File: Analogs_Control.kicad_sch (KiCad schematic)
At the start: 23 parts, among them U801 LM358

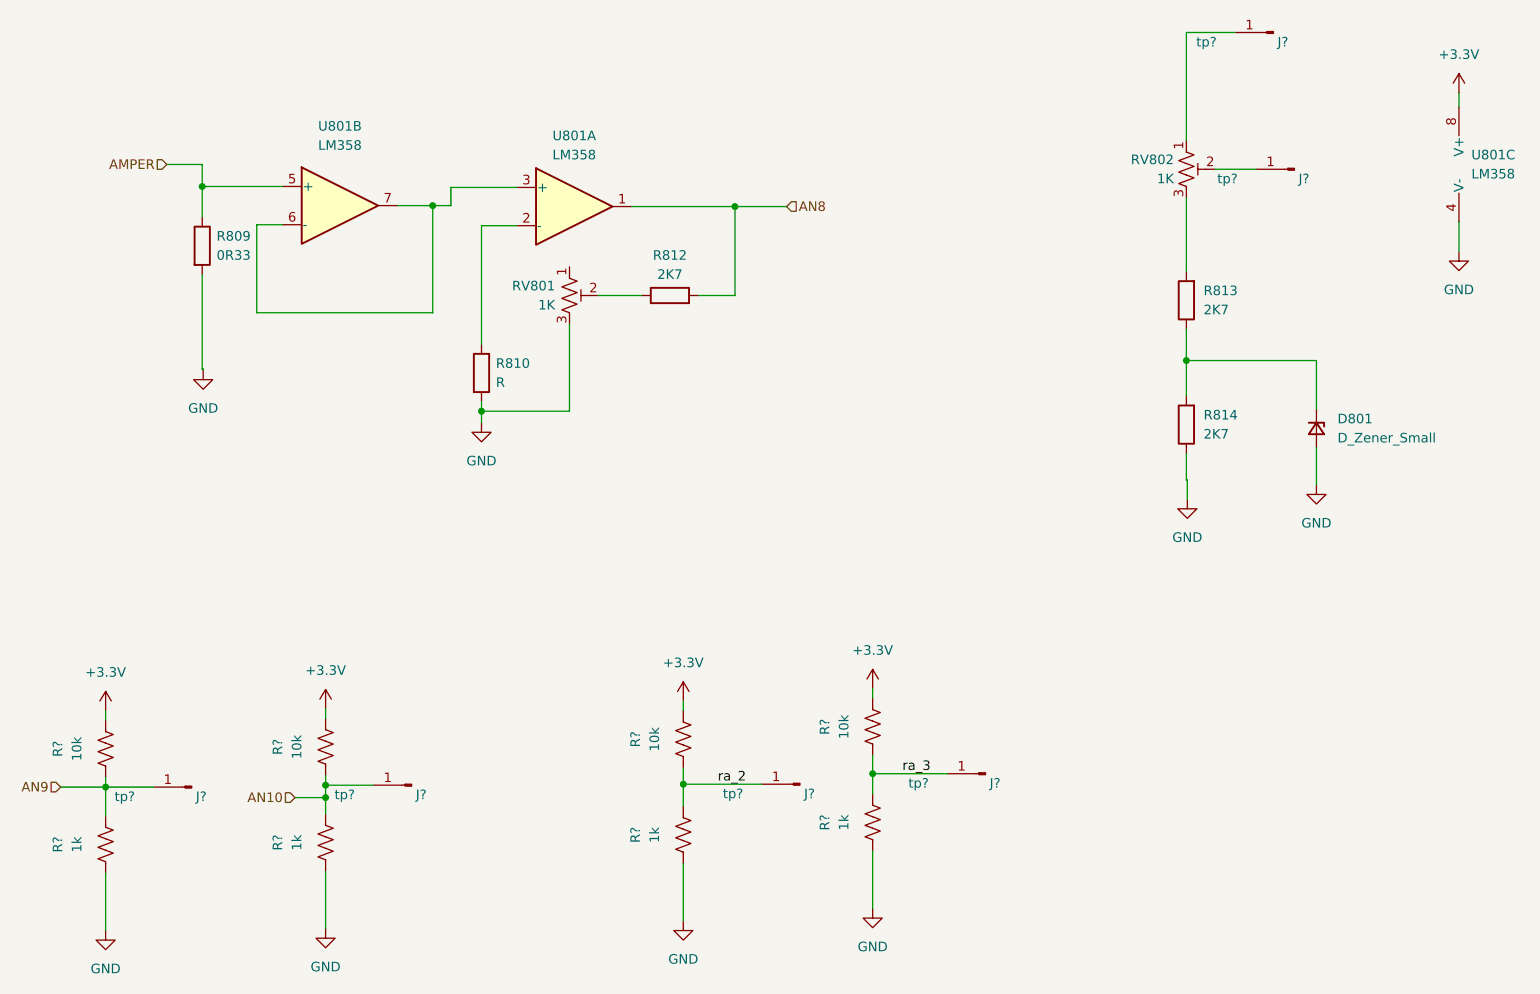
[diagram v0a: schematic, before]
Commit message: feat: agregar hierarchical_labels con nombres correctos a oS_AnaloDev (DiscoveryAnalog3) - 30 pines
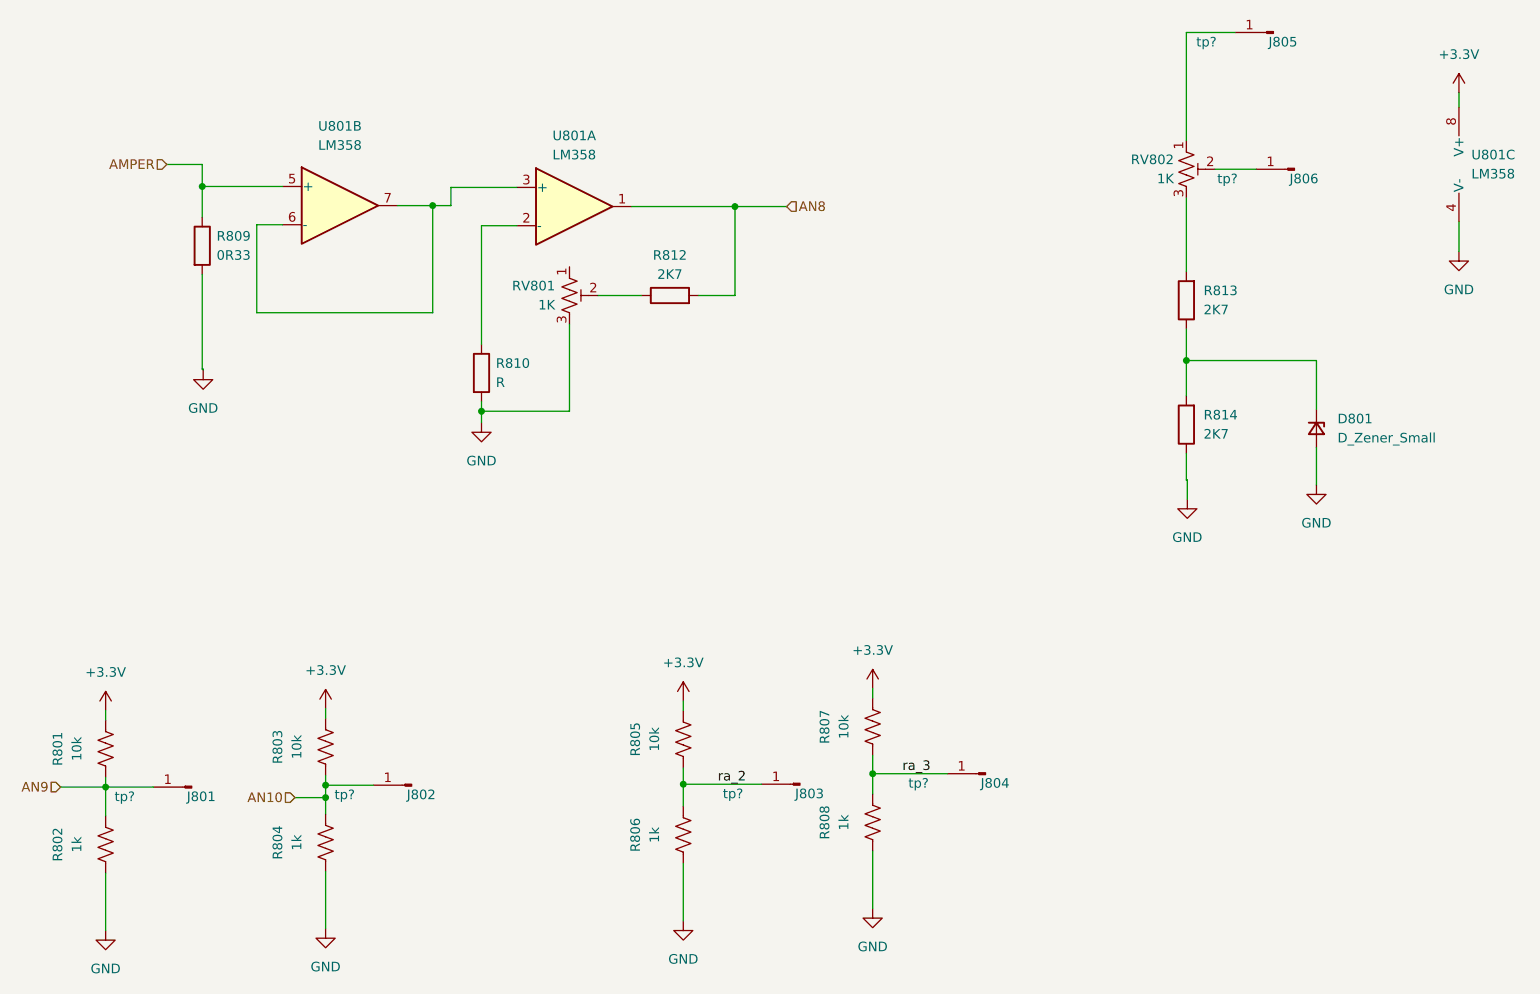
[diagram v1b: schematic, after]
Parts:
- gave numbers to parts that had none: 14
